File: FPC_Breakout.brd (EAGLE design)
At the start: 44.5 x 23.2 mm, 42 parts, among them IC1 MIC5335-SPYMT, IC2 MIC5335-MGYMT, IC3 TXS0108ERGY, SW1 PWRON, SW2 RESET, SW3 USER

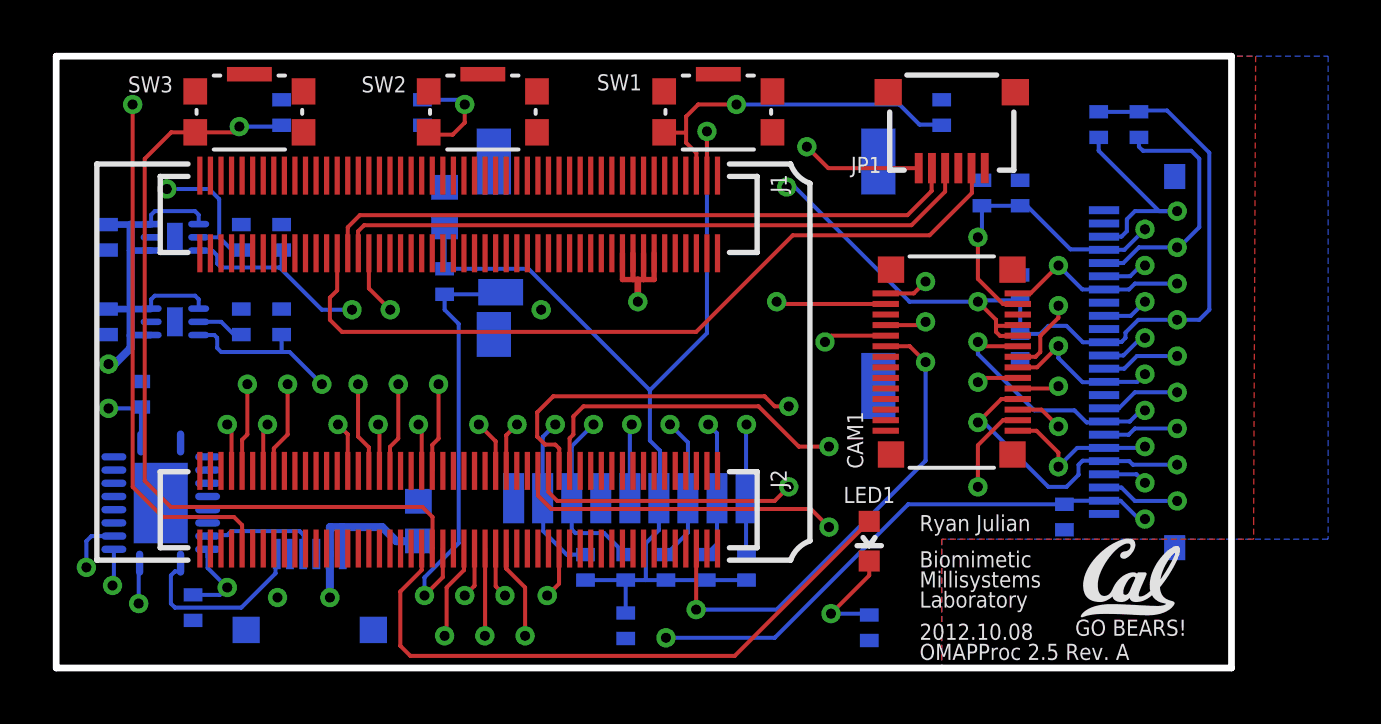
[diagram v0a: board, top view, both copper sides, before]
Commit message: Add FPC Breakout
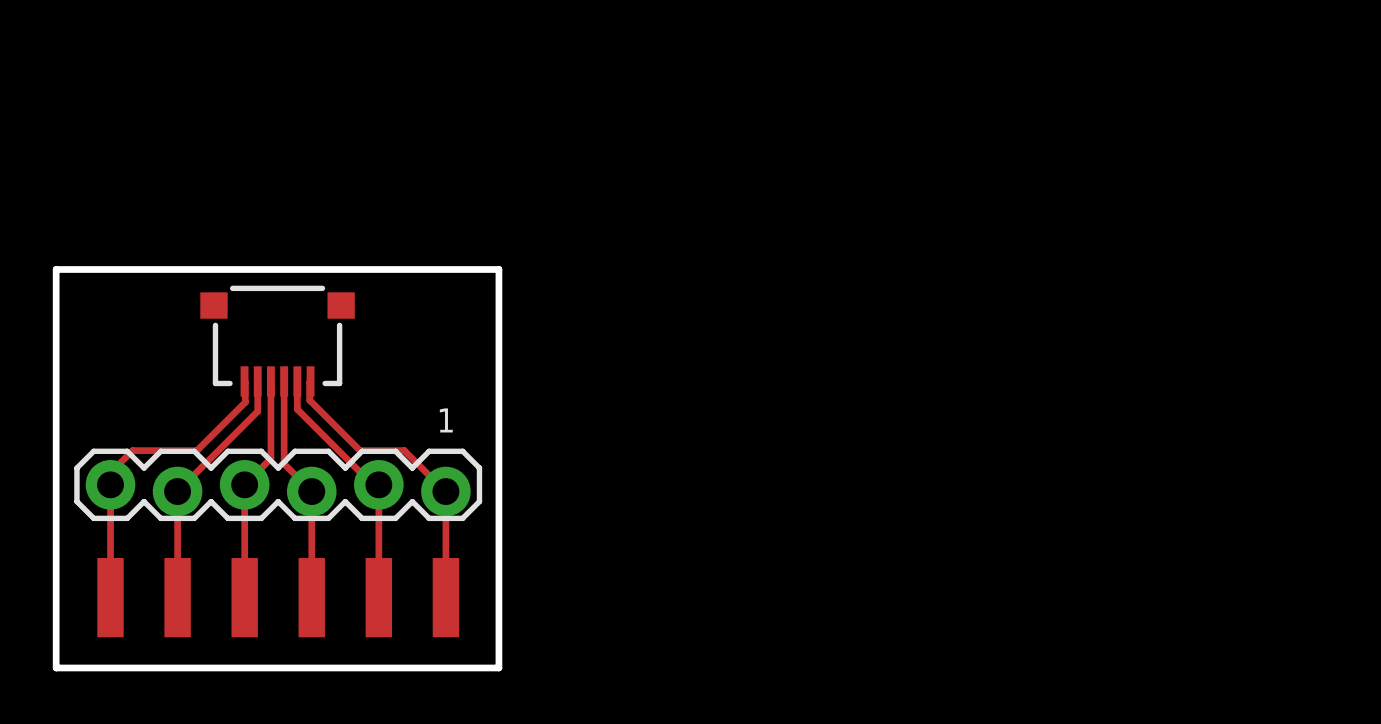
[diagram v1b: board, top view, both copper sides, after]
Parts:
- removed C1, C15, C16, C17, C2, C21, C22, C3, C8: 0.1uF, biomimetic:0402-CAP
- removed C10, C11, C12, C13, C14, C5, C6, C9: 1uF, biomimetic:0402-CAP
- removed C20, C7: 22uF, biomimetic:0603-CAP
- removed CAM1: LI-VM01CM, biomimetic:AXK7L28227G
- removed CAM2: ECAM50_5642_MOD, biomimetic:XF2W-2415-1A
- removed IC1: MIC5335-SPYMT, biomimetic:MLF-6
- removed IC2: MIC5335-MGYMT, biomimetic:MLF-6
- removed IC3: TXS0108ERGY, biomimetic:R-PVQFN-N20
- removed LED1: USER, biomimetic:LED-0603
- removed R1, R2: 1.5k, biomimetic:0402-RES
- removed R3, R4, R5, R6, R7: 10k, biomimetic:0402-RES
- removed R8: DNP, biomimetic:0402-RES
- removed R9: 330, biomimetic:0402-RES
- removed SDCARD1: MICROSD, biomimetic:AVX_045138008010890+
- removed SOM1: TORPEDO_DM3730, biomimetic:TORPEDO_DM3730
- removed SW1: PWRON, biomimetic:KMR421G
- removed SW2: RESET, biomimetic:KMR421G
- removed SW3: USER, biomimetic:KMR421G
- added JP3: (no value), SparkFun-Connectors:1X06-SMD_EDGE
- JP1: value CONSOLE -> MOLEX_503480-0600
- JP2: value IMAGEPROC -> (none); device biomimetic:MOLEX_503480-0600 -> SparkFun-Connectors:1X06-SIP_LOCK
- moved U$12 30.0 mm to (9.98, 10.4), flipped to the bottom
- moved JP1 26.8 mm to (8.38, 12.6)
- moved JP2 8.70 mm to (2.06, 6.93), flipped to the top
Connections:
- removed net !RESET: CAM1.20, CAM2.6, SOM1.J2.6
- removed net 1.8V: C1.2, C11.1, C15.1, C5.2, CAM1.10, CAM1.11, CAM2.11, IC2.5, IC3.10, IC3.2, R1.1, R2.1
- removed net 2.8V: C10.1, C3.1, C6.1, CAM1.13, CAM2.4, IC2.6
- removed net 3.0V: C14.1, IC1.5
- removed net 3.3V: C13.1, C16.1, C17.1, CAM2.23, IC1.6, IC3.19
- removed net CAM_D0: CAM1.1, CAM2.19, SOM1.J2.85
- removed net CAM_D1: CAM1.2, CAM2.21, SOM1.J2.87
- removed net CAM_D2: CAM1.3, CAM2.22, SOM1.J2.31
- removed net CAM_D3: CAM1.4, CAM2.20, SOM1.J2.33
- removed net CAM_D4: CAM1.5, CAM2.18, SOM1.J2.35
- removed net CAM_D5: CAM1.6, CAM2.16, SOM1.J2.29
- removed net CAM_D6: CAM1.7, CAM2.14, SOM1.J2.57
- removed net CAM_D7: CAM1.8, CAM2.12, SOM1.J2.55
- removed net CAM_HSYNC: CAM1.15, CAM2.9, SOM1.J2.63
- removed net CAM_MCLK: CAM1.16, CAM2.13, SOM1.J2.71
- removed net CAM_PCLK: CAM1.9, CAM2.17, SOM1.J2.67
- removed net CAM_SCLK: CAM1.19, CAM2.5, R1.2, SOM1.J2.93
- removed net CAM_SDATA: CAM1.18, CAM2.3, R2.2, SOM1.J2.91
- removed net CAM_VSYNC: CAM1.14, CAM2.7, SOM1.J2.65
- removed net GND: C1.1, C10.2, C11.2, C12.1, C13.2, C14.2, C15.2, C16.2, C17.2, C2.2, C20.2, C21.2, C22.2, C3.2, C5.1, C6.2, C7.2, C8.2, C9.1, CAM1.12, CAM1.17, CAM1.21, CAM2.15, CAM2.2, CAM2.24, CAM2.8, IC1.2, IC1.EPAD, IC2.2, IC2.EPAD, IC3.11, IC3.EPAD, JP1.1, JP2.3, JP2.5, R9.2, SDCARD1.6, SDCARD1.CASE1, SDCARD1.CASE2, SDCARD1.CASE3, SDCARD1.CASE4, SDCARD1.COM, SOM1.J1.100, SOM1.J1.12, SOM1.J1.17, SOM1.J1.22, SOM1.J1.27, SOM1.J1.61, SOM1.J1.85, SOM1.J2.1, SOM1.J2.2, SOM1.J2.27, SOM1.J2.30, SOM1.J2.59, SOM1.J2.62, SOM1.J2.90, SOM1.J2.99, SW1.3, SW1.4, SW1.CASE, SW2.3, SW2.4, SW2.CASE, SW3.3, SW3.4, SW3.CASE
- removed net MSTR_NRST: C21.1, SOM1.J2.92, SW2.1, SW2.2
- removed net N$1: SOM1.J1.24
- removed net N$2: SOM1.J2.4, SOM1.J2.7
- removed net N$3: LED1.C, R9.1
- removed net PWRON: C22.1, SOM1.J1.5, SW1.1, SW1.2
- removed net SD1_CD: R8.1, SDCARD1.CD, SOM1.J2.54
- removed net SD1_CLK: SDCARD1.5, SOM1.J2.32
- removed net SD1_CMD: R3.1, SDCARD1.3, SOM1.J2.42
- removed net SD1_DATA0: R4.1, SDCARD1.7, SOM1.J2.48
- removed net SD1_DATA1: R5.1, SDCARD1.8, SOM1.J2.46
- removed net SD1_DATA2: R6.1, SDCARD1.1, SOM1.J2.44
- removed net SD1_DATA3: R7.1, SDCARD1.2, SOM1.J2.50
- removed net UARTA_CTS: JP1.6, SOM1.J1.68
- removed net UARTA_RTS: JP1.2, SOM1.J1.74
- removed net UARTA_RX: JP1.4, SOM1.J1.70
- removed net UARTA_TX: JP1.5, SOM1.J1.72
- removed net UARTB_RX: IC3.3, SOM1.J2.41
- removed net UARTB_RX_3V3: IC3.18, JP2.4
- removed net UARTB_TX: IC3.1, SOM1.J2.43
- removed net UARTB_TX_3V3: IC3.20, JP2.6
- removed net USER_LED: LED1.A, SOM1.J2.58
- removed net USER_SW: C2.1, SOM1.J2.56, SW3.1, SW3.2
- removed net VMMC1: C7.1, C8.1, R3.2, R4.2, R5.2, R6.2, R7.2, R8.2, SDCARD1.4, SOM1.J1.3
- removed net V_BATT: C12.2, C20.1, C9.2, IC1.1, IC1.3, IC1.4, IC2.1, IC2.3, IC2.4, JP2.1, JP2.2, SOM1.J1.14, SOM1.J1.16, SOM1.J1.18, SOM1.J1.20
- new net PIN1: JP1.1, JP2.6, JP3.6
- new net PIN2: JP1.2, JP2.5, JP3.5
- new net PIN3: JP1.3, JP2.4, JP3.4
- new net PIN4: JP1.4, JP2.3, JP3.3
- new net PIN5: JP1.5, JP2.2, JP3.2
- new net PIN6: JP1.6, JP2.1, JP3.1
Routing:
- net 1.8V: track 83.4 -> 0.00 mm, vias 6 -> 0
- net 3.3V: track 57.5 -> 0.00 mm, vias 4 -> 0
- net CAM_SCLK: track 53.9 -> 0.00 mm, vias 3 -> 0
- net CAM_SDATA: track 53.6 -> 0.00 mm, vias 3 -> 0
- net CAM_D0: track 49.9 -> 0.00 mm, vias 3 -> 0
- net CAM_D1: track 48.4 -> 0.00 mm, vias 3 -> 0
- net CAM_MCLK: track 45.2 -> 0.00 mm, vias 3 -> 0
- net 2.8V: track 44.4 -> 0.00 mm, vias 3 -> 0
- net CAM_VSYNC: track 44.3 -> 0.00 mm, vias 3 -> 0
- net VMMC1: track 38.5 -> 0.00 mm, vias 1 -> 0
- net CAM_HSYNC: track 38.4 -> 0.00 mm, vias 3 -> 0
- net CAM_PCLK: track 37.2 -> 0.00 mm, vias 3 -> 0
- net MSTR_NRST: track 37.1 -> 0.00 mm, vias 2 -> 0
- net CAM_D7: track 36.7 -> 0.00 mm, vias 3 -> 0
- net CAM_D2: track 34.0 -> 0.00 mm, vias 3 -> 0
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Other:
- board size 44.5 x 23.2 mm -> 16.8 x 15.1 mm
- board text added: "1"
- board text added: "FPC Breakout Rev. A"
- board text removed: "OMAPProc 2.5 Rev. A"
